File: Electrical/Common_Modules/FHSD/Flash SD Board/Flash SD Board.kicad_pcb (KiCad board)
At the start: 2 copper layers, 27.9 x 25.8 mm, 5 parts, among them J501 Conn_01x07_Male, U10 W25N512GVPIT

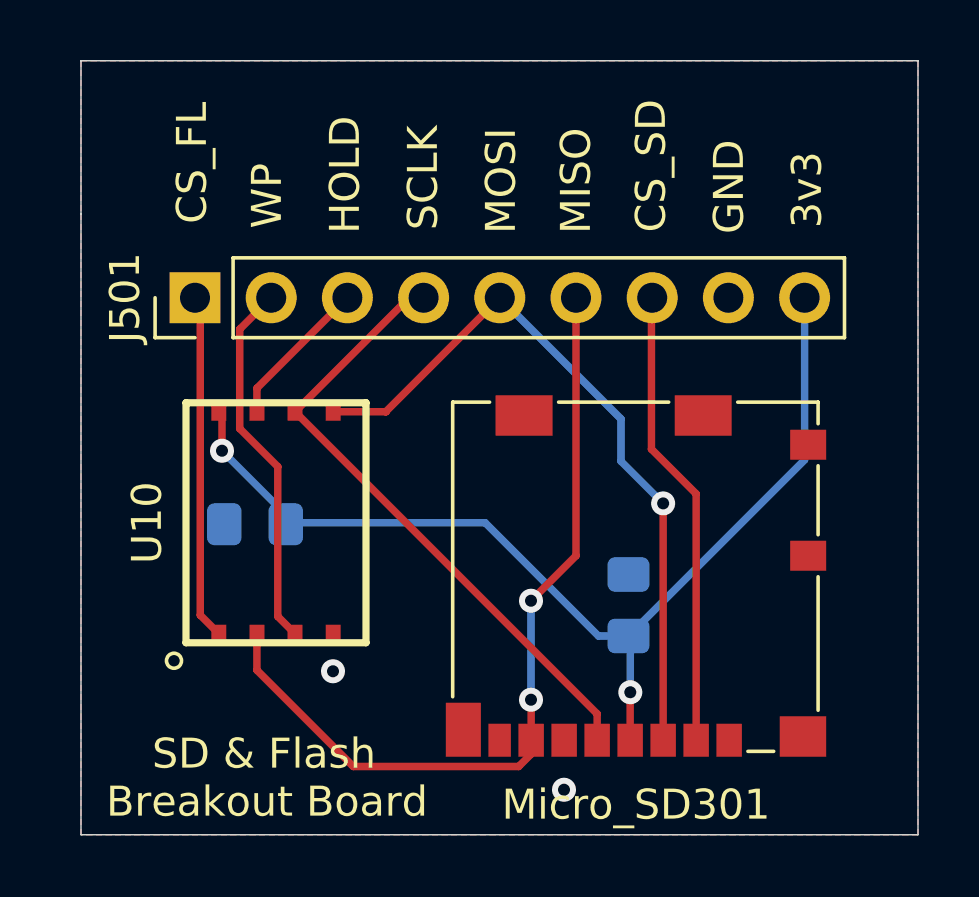
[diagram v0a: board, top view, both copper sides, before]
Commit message: Fixed Flash chip footprint
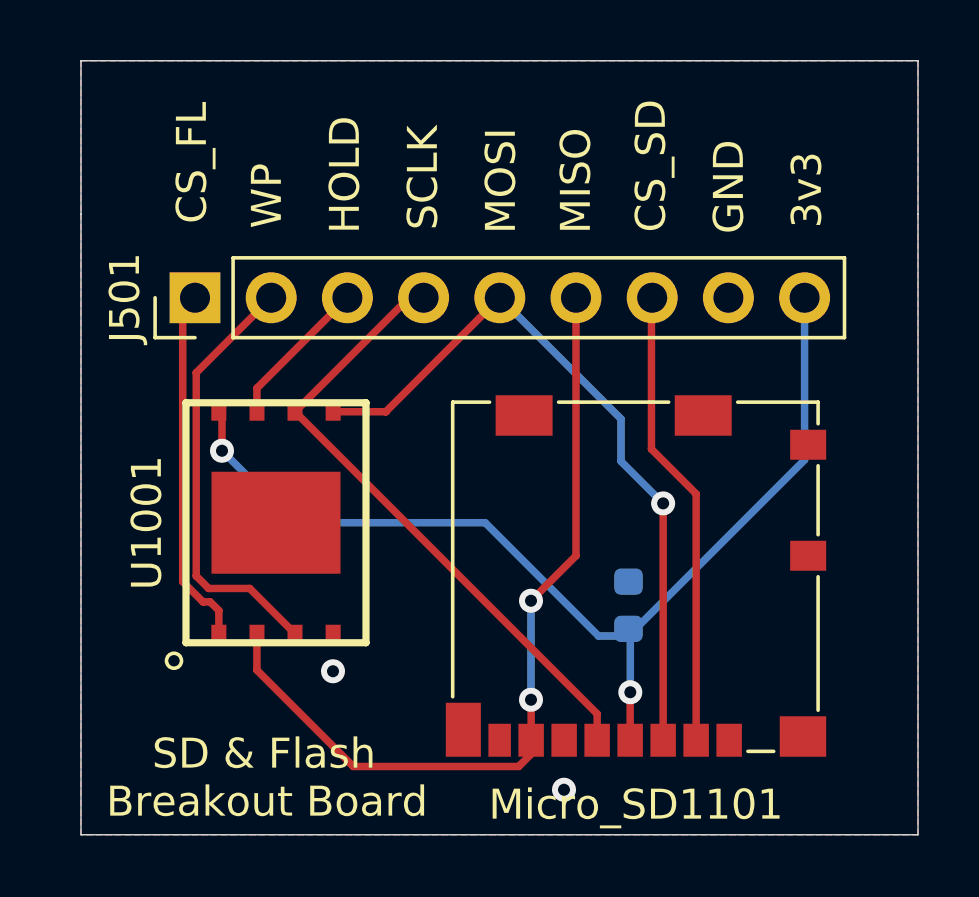
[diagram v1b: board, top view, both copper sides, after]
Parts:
- C1001: renamed from C401; footprint Capacitor_SMD:C_0805_2012Metric_Pad1.15x1.40mm_HandSolder -> NOVA MCU (STM):C_0603_1608Metric
- C301: footprint Capacitor_SMD:C_0805_2012Metric_Pad1.15x1.40mm_HandSolder -> NOVA MCU (STM):C_0603_1608Metric
- U1001: renamed from U10; footprint Footprint Library:W25N512GVPIT -> FCSD:W25N512GVPIT
- renumbered Micro_SD301 to Micro_SD1101
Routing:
- net /main/Flash Chip/WP: track 12.4 -> 14.4 mm
